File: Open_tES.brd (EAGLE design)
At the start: 105.2 x 98 mm, 60 parts, among them IC2 MAX232ECWES, IC4 LP2950CZ-5.0, IC5 OPA277U, IC6 LF444CM, IC7 PIC16F1937P, J1 RJ11-2X, U1 MIC2288YD5-TR, U2 74LVC1G10W6-7, X1 22-23-2041, X2 057-016-1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

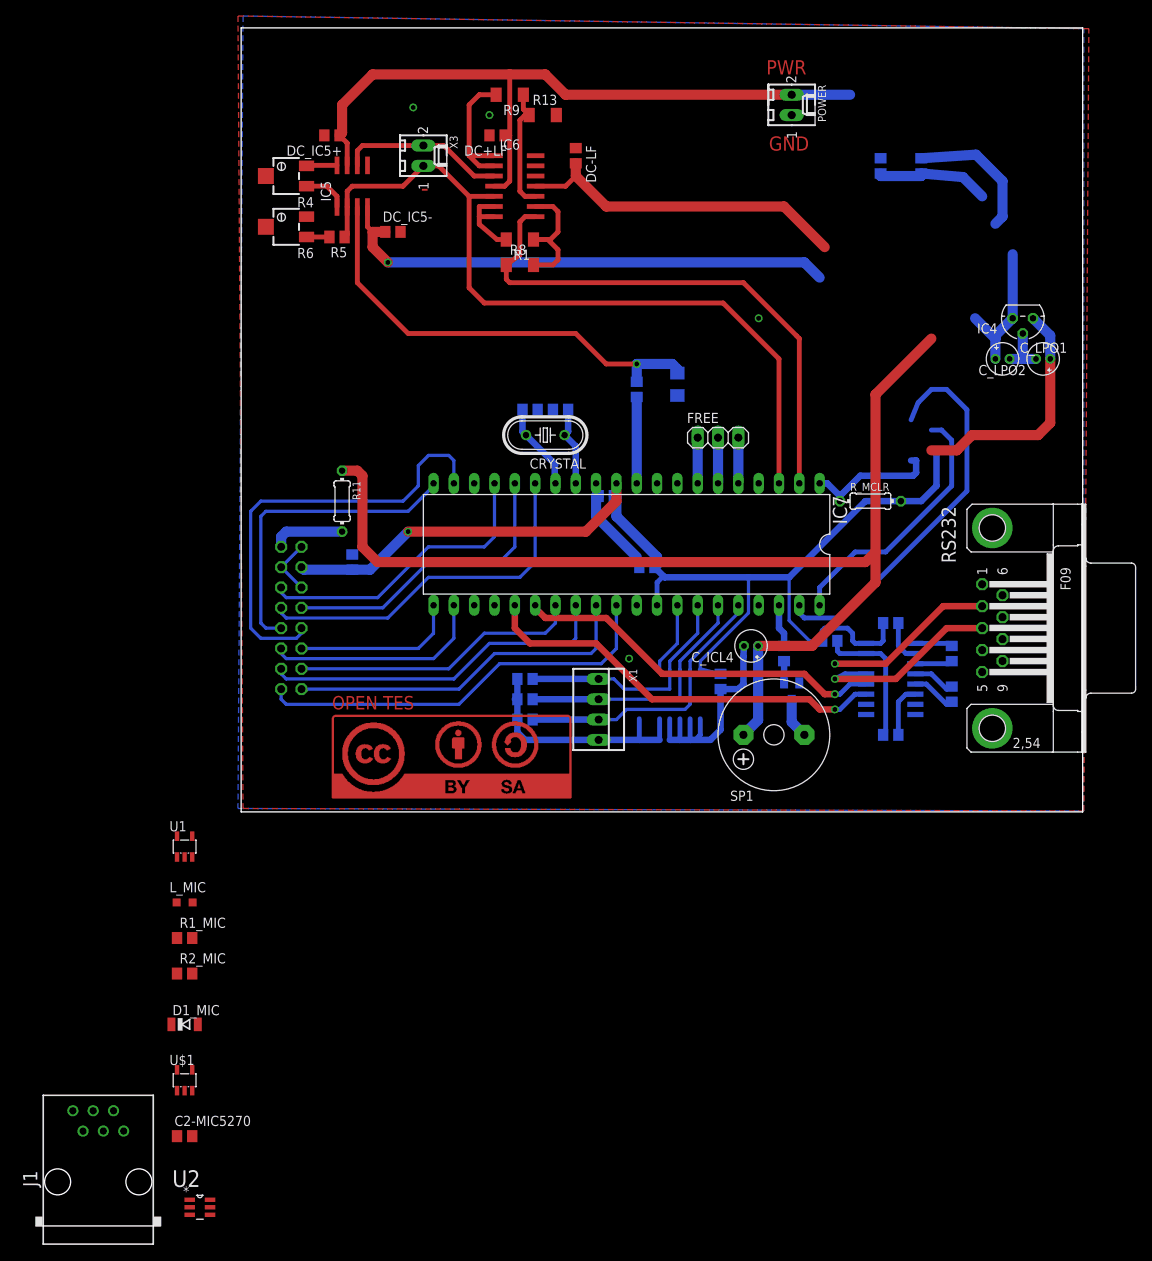
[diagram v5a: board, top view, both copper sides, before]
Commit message: fixing of connecting error +9V and +30V. MIC2288 and LP2950 was concerned. Correction of capacitor for LPO.
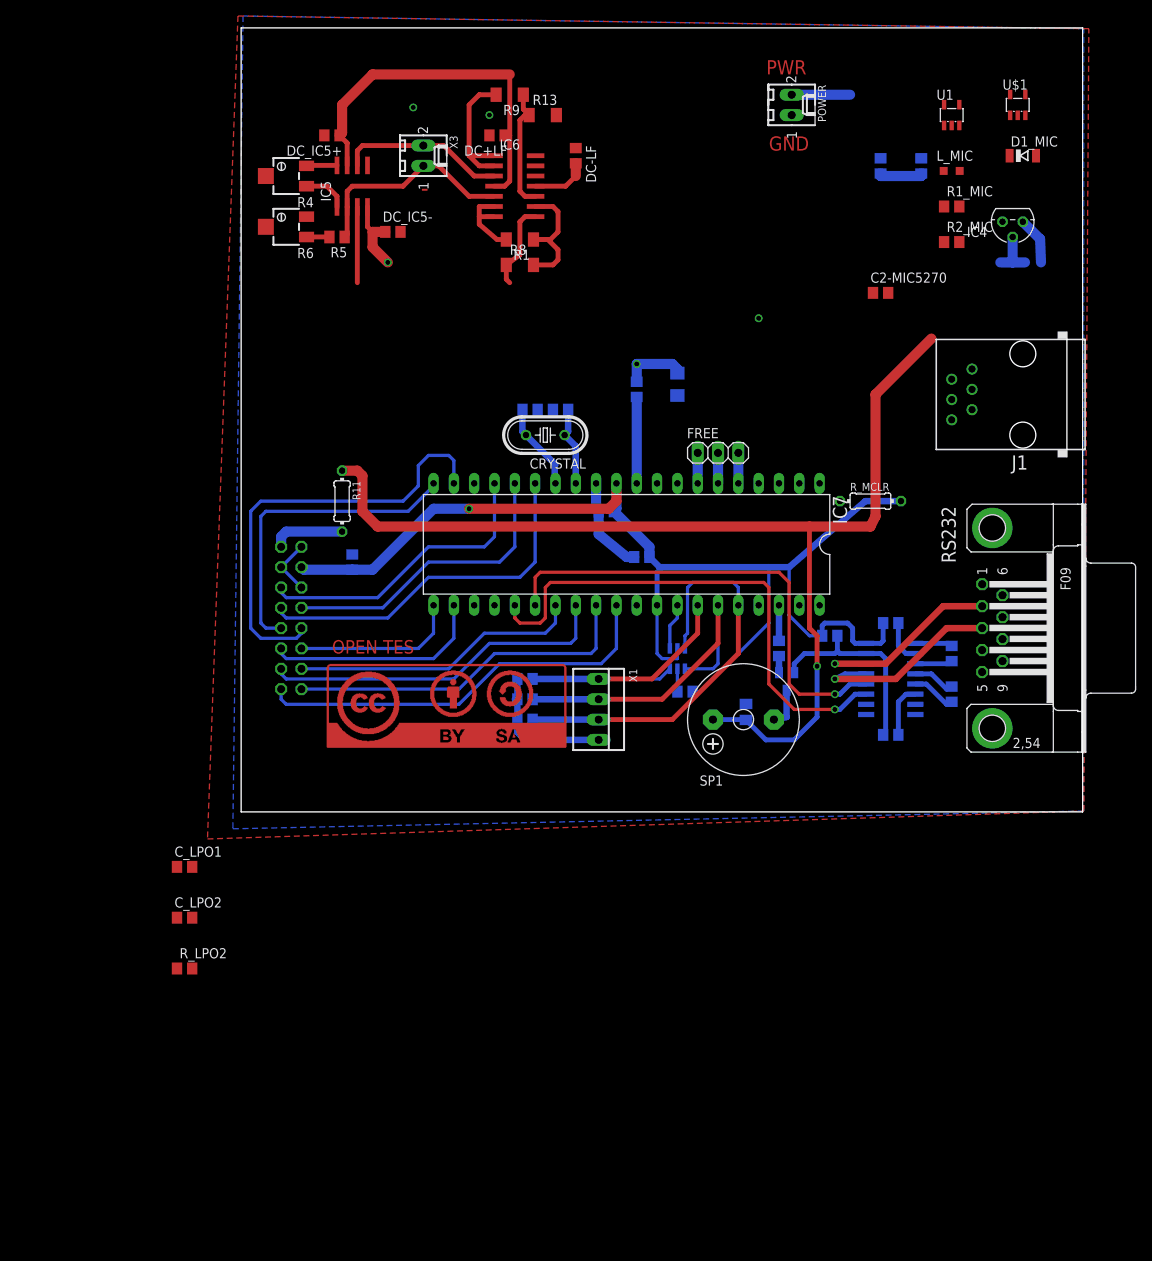
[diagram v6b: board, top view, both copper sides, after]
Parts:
- added R_LPO2: 1R, rcl:R0805
- C_ICL4: device rcl:E1,8-4 -> rcl:C0805K
- C_LPO1, C_LPO2: value 2.2µF -> 1µF; device rcl:E1,8-4 -> rcl:C0805
- moved U$1 160.3 mm to (95.9, 79.4)
- moved J1 151.8 mm to (96.5, 43.2), turned to 90 degrees
- moved D1_MIC 150.9 mm to (96.5, 73.0)
- moved C2-MIC5270 136.7 mm to (78.7, 55.9)
- moved L_MIC 132.5 mm to (87.6, 71.1)
- moved R1_MIC 132.5 mm to (87.6, 66.7)
- moved R2_MIC 132.5 mm to (87.6, 62.2)
- moved U1 132.5 mm to (87.6, 78.1)
- moved C_LPO2 128.0 mm to (-8.26, -22.2), turned to 0 degrees
- moved C_LPO1 120.4 mm to (-8.26, -15.9)
- moved U2 90.9 mm to (53.3, 10.2), flipped to the bottom, turned to 90 degrees
- moved IC4 12.1 mm to (95.2, 64.8)
- moved C_ICL4 8.28 mm to (61.9, 3.49), flipped to the bottom, turned to 90 degrees
- moved U$4 6.98 mm to (10.2, 10.8)
- moved U$2 6.38 mm to (9.53, -0.95)
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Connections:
- new net N$21: C_LPO2.1, R_LPO2.1
- net +24V: now also C2_MIC.1, D1_MIC.C, R1_MIC.2; no longer C1_MIC.1, L_MIC.1, POWER.2, U1.4, U1.5
- net +5V/1: now also R_LPO2.2; no longer C_LPO2.+
- net +9V: now also C1_MIC.1, C_ICL4.1, C_LPO1.1, L_MIC.1, POWER.2, U1.4, U1.5; no longer C2_MIC.1, C_ICL4.+, C_LPO1.+, D1_MIC.C, R1_MIC.2
- net GND: now also C_ICL4.2, C_LPO1.2, C_LPO2.2; no longer C_ICL4.-, C_LPO1.-, C_LPO2.-
- net N$23: now also U2.1; no longer U2.3
- net N$9: now also U2.3; no longer U2.1
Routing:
- net -5V: track 106.3 -> 16.7 mm
- net ICAPT: track 96.5 -> 27.1 mm
- net UCAPT: track 68.1 -> 10.9 mm
- net PGC: track 49.1 -> 0.00 mm
- net +24V: track 90.4 -> 46.8 mm
- net GND: track 117.6 -> 77.1 mm, vias 4 -> 3
- net N$19: track 56.7 -> 17.5 mm
- net PGD: track 32.8 -> 0.00 mm
- net +9V: track 175.2 -> 144.8 mm, vias 0 -> 1
- net +5V/1: track 176.3 -> 157.2 mm
- net MCLR: track 16.7 -> 0.00 mm
- net N$18: track 35.4 -> 52.0 mm
- net N$11: track 51.8 -> 64.5 mm
- net N$15: track 46.7 -> 59.4 mm
- net N$23: track 32.1 -> 42.5 mm
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
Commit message: Removing input capacitor for LPO: C1_MIC already present.
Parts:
- removed C_LPO1: 1µF, rcl:C0805
- moved R_LPO2 133.6 mm to (95.2, 55.9), flipped to the bottom, turned to 180 degrees
- moved C_LPO2 125.6 mm to (90.2, 55.9), flipped to the bottom
- moved U$1 44.0 mm to (57.1, 58.4), flipped to the bottom
- moved C2-MIC5270 26.2 mm to (52.7, 58.4), flipped to the bottom, turned to 90 degrees
- moved C1_MIC 13.9 mm to (91.4, 77.5), turned to 0 degrees
- moved R2_MIC 13.0 mm to (85.1, 74.9), flipped to the bottom
- moved D1_MIC 11.4 mm to (85.7, 69.2), flipped to the bottom, turned to 180 degrees
- moved R1_MIC 11.1 mm to (85.1, 77.5), flipped to the bottom, turned to 180 degrees
- moved U1 5.85 mm to (91.4, 73.7), flipped to the bottom, turned to 90 degrees
- moved IC4 4.62 mm to (94.0, 60.3)
- moved L_MIC 4.26 mm to (91.4, 69.2), flipped to the bottom
- moved C2_MIC 1.42 mm to (85.1, 72.4), turned to 180 degrees
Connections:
- net +9V: no longer C_LPO1.1
- net GND: no longer C_LPO1.2
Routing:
- net GND: track 77.1 -> 65.1 mm, vias 3 -> 2
- net +9V: track 144.8 -> 138.9 mm
- net N$21: track 0.00 -> 3.18 mm
- net +5V/1: track 157.2 -> 156.4 mm

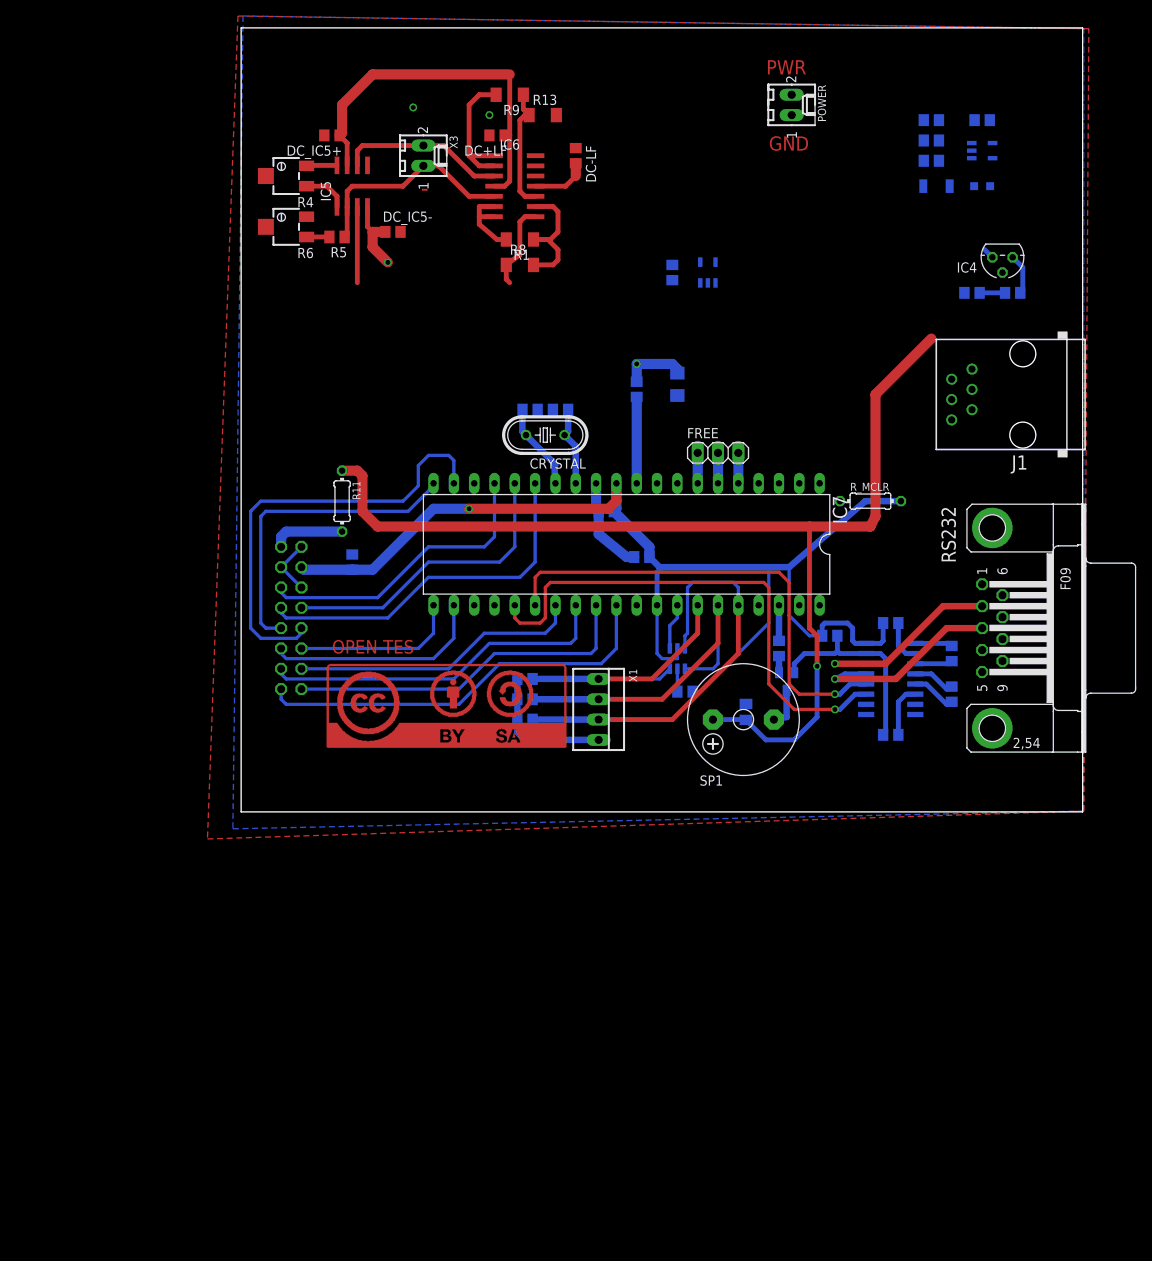
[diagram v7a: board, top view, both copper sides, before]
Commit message: Adding of state of charge module connecting to AN4: firmware updating is necessary. End of routing
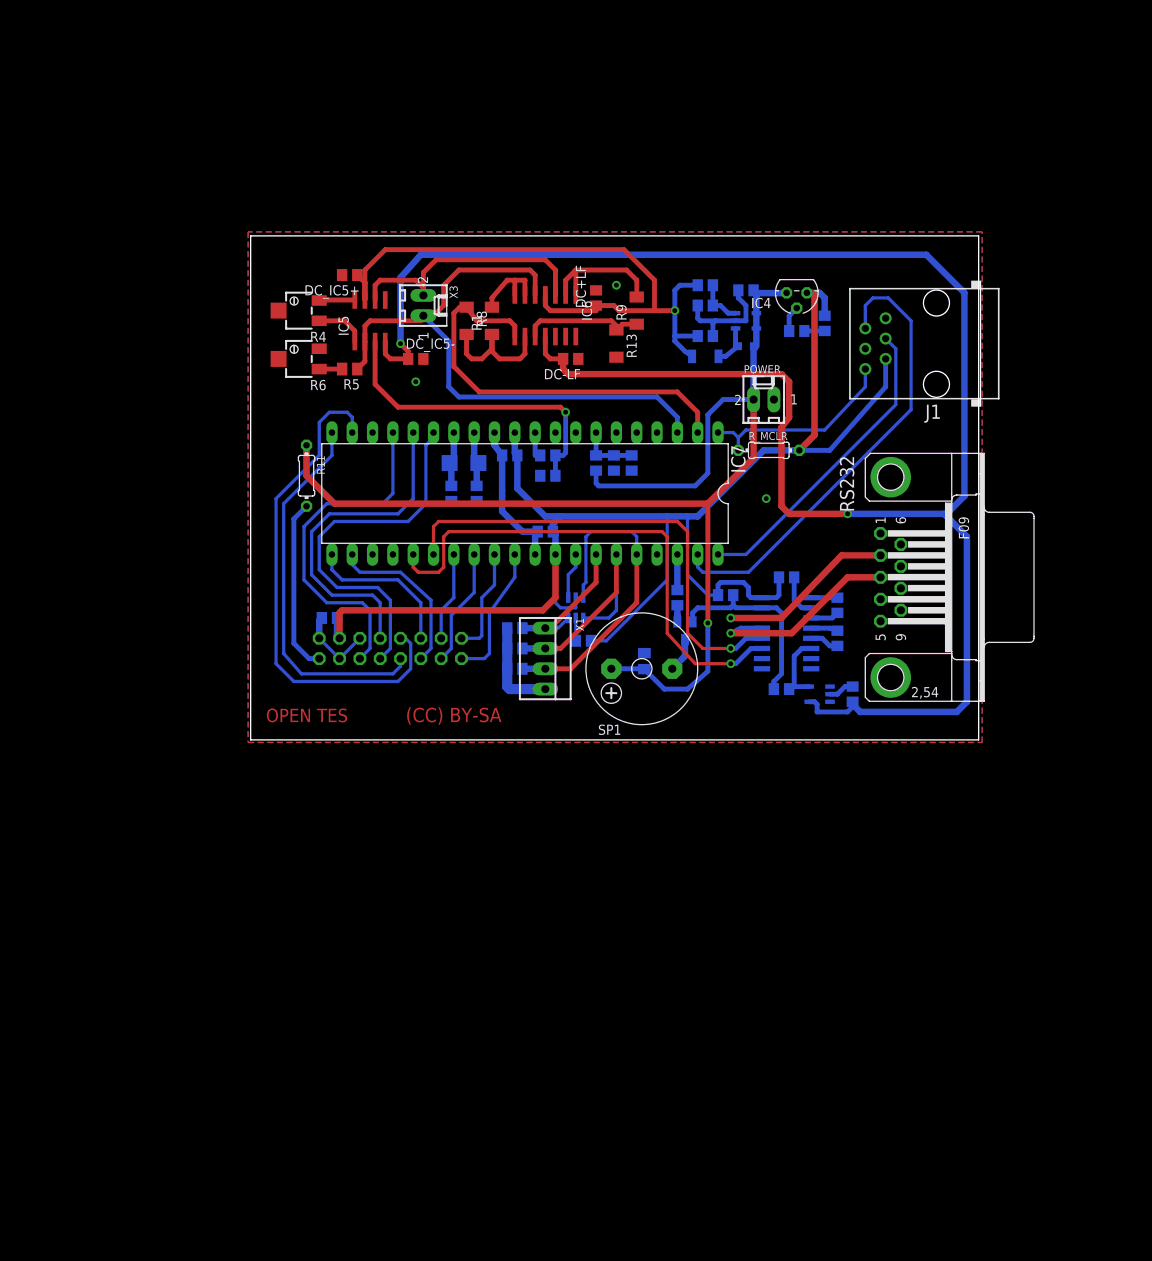
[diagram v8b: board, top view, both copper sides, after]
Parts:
- removed CRYSTAL: 32MHz, crystal:HC49U-V
- removed FREE: (no value), pinhead:1X03
- removed U$2: (no value), logo:BY-SA
- added C_SOC: 0.1µF, rcl:C0805
- added R_SOC1, R_SOC2: 51K, rcl:R0805
- added U$3: QC5CB, Open_tES:QC5CB
- C_FILT: device rcl:C1206 -> rcl:C0805
- moved C2-MIC5270 57.3 mm to (75.2, 5.71), turned to 270 degrees
- moved U$1 54.5 mm to (71.1, 5.71), turned to 270 degrees
- moved POWER 37.0 mm to (64.1, 42.5), turned to 0 degrees
- moved C1_MIC 36.4 mm to (61.9, 56.2)
- moved U1 36.4 mm to (61.9, 52.4)
- moved D1_MIC 35.9 mm to (56.8, 47.9)
- moved C2_MIC 35.8 mm to (56.8, 50.5)
- moved L_MIC 35.7 mm to (61.9, 49.2)
- moved R2_MIC 35.0 mm to (56.8, 54.3), turned to 180 degrees
- moved R1_MIC 35.0 mm to (56.8, 56.8), turned to 0 degrees
- moved R9 31.3 mm to (48.3, 53.7), turned to 90 degrees
- moved R13 30.0 mm to (45.7, 49.5), turned to 270 degrees
- moved IC4 26.1 mm to (68.3, 55.9)
- moved DC-LF 25.4 mm to (40.0, 47.6), turned to 180 degrees
- moved R_LPO2 23.8 mm to (71.8, 52.1), turned to 90 degrees
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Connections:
- net +24V renamed +30V
- removed net N$24: FREE.1, IC7.7
- removed net N$26: FREE.2, IC7.6
- removed net N$34: FREE.3, IC7.5
- new net AN4: C_SOC.1, IC7.7, R_SOC1.1, R_SOC2.2
- net +9V: now also R_SOC1.2
- net GND: now also C_SOC.2, R_SOC2.1; no longer IC7.4
- net N$20: now also U$3.1; no longer CRYSTAL.1
- net N$6: now also U$3.2; no longer CRYSTAL.2
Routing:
- net -5V: track 16.7 -> 236.3 mm, vias 1 -> 2
- net PGC: track 0.00 -> 58.2 mm
- net ICAPT: track 27.1 -> 76.6 mm
- net UCAPT: track 10.9 -> 52.4 mm
- net PGD: track 0.00 -> 38.8 mm
- net +30V: track 46.8 -> 83.8 mm, vias 0 -> 1
- net +5V/1: track 156.4 -> 191.4 mm, vias 1 -> 0
- net LCD7: track 51.7 -> 17.2 mm
- net LCD6: track 44.3 -> 13.5 mm
- net LCD5: track 44.0 -> 14.7 mm
- net MCLR: track 0.00 -> 25.2 mm
- net LCD4: track 36.3 -> 11.1 mm
- net GND: track 65.1 -> 88.2 mm, vias 2 -> 3
- net N$19: track 17.5 -> 39.6 mm
- net N$9: track 35.6 -> 16.9 mm
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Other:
- board size 105.2 x 98 mm -> 91 x 63 mm
- board text added: "(CC) BY-SA"
- board text removed: "-"
- board text removed: "GND"
- board text removed: "PWR"
